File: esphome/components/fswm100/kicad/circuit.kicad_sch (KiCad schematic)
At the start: 17 parts, among them J1 Bi-Directional 3.3V-5V Shifte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, J2 ESP32 DEVKITV1 (ESP-WROOM-32), U1 ADS1115IDGS, U2 L7805, U3 TCRT5000, U4 L7805

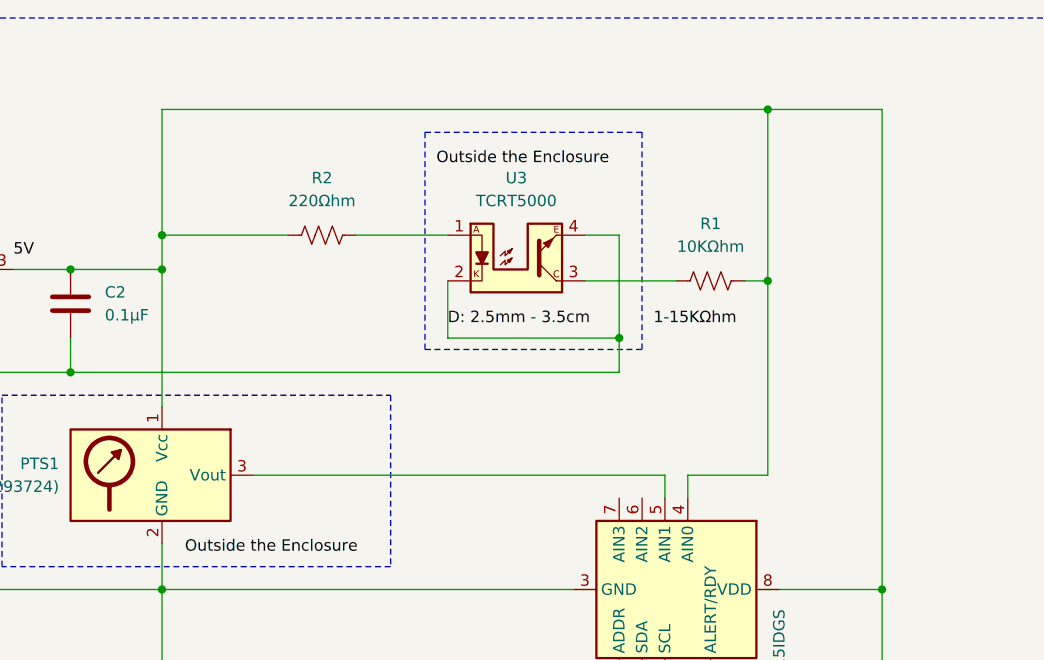
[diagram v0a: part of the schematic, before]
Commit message: fix flow sensor code and diagram
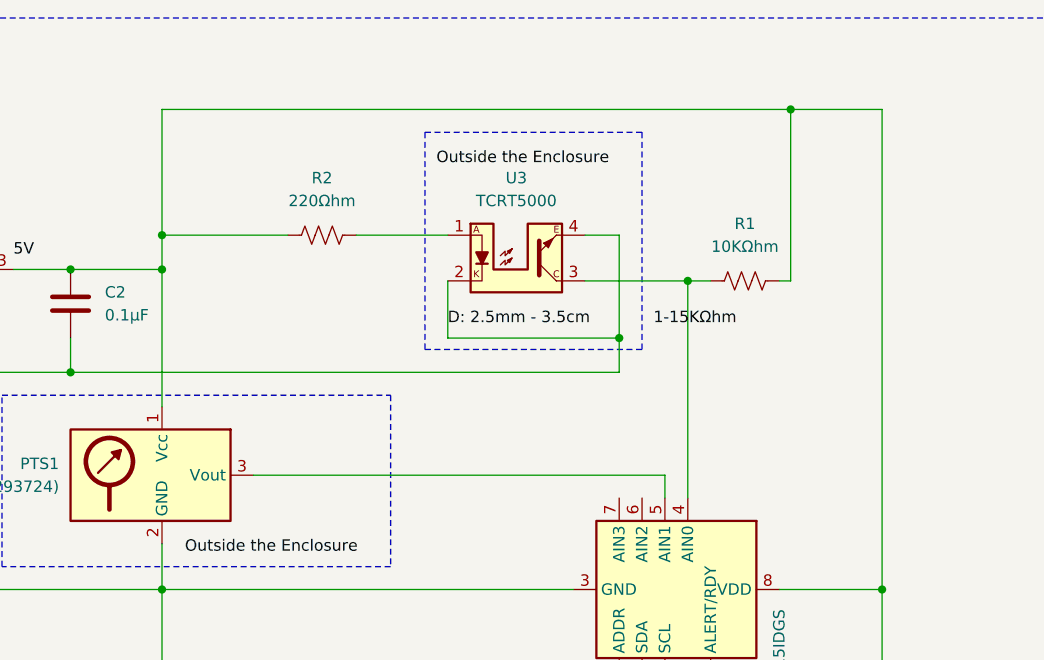
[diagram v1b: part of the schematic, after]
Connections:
- net at C2.1, J1.HV (3), PTS1.1 (Vcc)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: no longer U1.4 (AIN0)
- net at R1.2, U3.3: now also U1.4 (AIN0)
- new net: J1.GND (9), J2.GND (Pin_17), R3.2
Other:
- moved on the sheet: R1
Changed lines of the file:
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@@
-	)
-	(junction
-		(at 157.48 64.77)
-		(diameter 0)
-		(color 0 0 0 0)
 	)
 	(junction
@@
 	)
 	(junction
+		(at 148.59 64.77)
+		(diameter 0)
+		(color 0 0 0 0)
+	)
+	(junction
 		(at 39.37 74.93)
 		(diameter 0)
@@
 	)
 	(junction
-		(at 157.48 45.72)
-		(diameter 0)
-		(color 0 0 0 0)
-	)
-	(junction
 		(at 170.18 99.06)
 		(diameter 0)
@@
 	)
 	(junction
+		(at 160.02 45.72)
+		(diameter 0)
+		(color 0 0 0 0)
+	)
+	(junction
 		(at 49.53 74.93)
 		(diameter 0)
@@
 	(wire
 		(pts
-			(xy 137.16 64.77) (xy 147.32 64.77)
+			(xy 137.16 64.77) (xy 148.59 64.77)
 		)
 		(stroke
@@
 	(wire
 		(pts
+			(xy 151.13 64.77) (xy 148.59 64.77)
+		)
+		(stroke
+			(width 0)
+			(type default)
+		)
+	)
+	(wire
+		(pts
 			(xy 73.66 63.5) (xy 80.01 63.5)
 		)
@@
 	(wire
 		(pts
-			(xy 157.48 45.72) (xy 90.17 45.72)
+			(xy 90.17 45.72) (xy 160.02 45.72)
 		)
 		(stroke
@@
 	(wire
 		(pts
+			(xy 148.59 64.77) (xy 148.59 88.9)
+		)
+		(stroke
+			(width 0)
+			(type default)
+		)
+	)
+	(wire
+		(pts
 			(xy 236.22 151.13) (xy 261.62 151.13)
 		)
@@
 	(wire
 		(pts
-			(xy 148.59 88.9) (xy 148.59 86.36)
-		)
-		(stroke
-			(width 0)
-			(type default)
-		)
-	)
-	(wire
-		(pts
 			(xy 66.04 99.06) (xy 66.04 74.93)
 		)
@@
 	(wire
 		(pts
-			(xy 157.48 86.36) (xy 157.48 64.77)
-		)
-		(stroke
-			(width 0)
-			(type default)
-		)
-	)
-	(wire
-		(pts
 			(xy 257.81 59.69) (xy 261.62 59.69)
 		)
@@
 	(wire
 		(pts
-			(xy 157.48 45.72) (xy 170.18 45.72)
-		)
-		(stroke
-			(width 0)
-			(type default)
-		)
-	)
-	(wire
-		(pts
 			(xy 90.17 78.74) (xy 90.17 63.5)
 		)
@@
 	(wire
 		(pts
-			(xy 154.94 64.77) (xy 157.48 64.77)
+			(xy 158.75 64.77) (xy 160.02 64.77)
 		)
 		(stroke
@@
 	(wire
 		(pts
-			(xy 157.48 64.77) (xy 157.48 45.72)
+			(xy 160.02 64.77) (xy 160.02 45.72)
 		)
 		(stroke
@@
 	(wire
 		(pts
+			(xy 160.02 45.72) (xy 170.18 45.72)
+		)
+		(stroke
+			(width 0)
+			(type default)
+		)
+	)
+	(wire
+		(pts
 			(xy 170.18 130.81) (xy 170.18 99.06)
-		)
-		(stroke
-			(width 0)
-			(type default)
-		)
-	)
-	(wire
-		(pts
-			(xy 148.59 86.36) (xy 157.48 86.36)
 		)
 		(stroke
@@
 	(symbol
 		(lib_id "Device:R_US")
-		(at 151.13 64.77 270)
+		(at 154.94 64.77 270)
 		(unit 1)
 		(exclude_from_sim no)
@@
 		(fields_autoplaced yes)
 		(property "Reference" "R1"
-			(at 151.13 58.42 90)
+			(at 154.94 58.42 90)
 			(effects
 				(font
@@
 		)
 		(property "Value" "10KΩhm"
-			(at 151.13 60.96 90)
+			(at 154.94 60.96 90)
 			(effects
 				(font
@@
 		)
 		(property "Footprint" ""
-			(at 150.876 65.786 90)
+			(at 154.686 65.786 90)
 			(effects
 				(font
@@
 		)
 		(property "Datasheet" "~"
-			(at 151.13 64.77 0)
+			(at 154.94 64.77 0)
 			(effects
 				(font
@@
 		)
 		(property "Description" "Resistor, US symbol"
-			(at 151.13 64.77 0)
+			(at 154.94 64.77 0)
 			(effects
 				(font

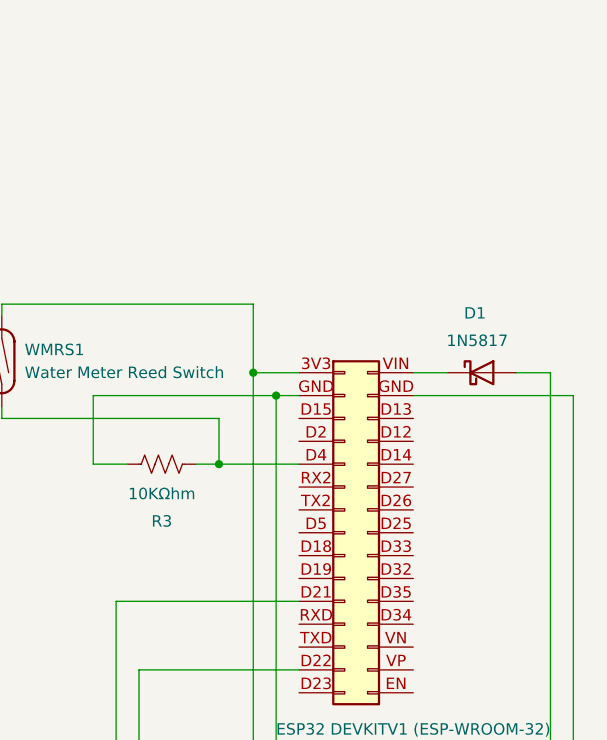
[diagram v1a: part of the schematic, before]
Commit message: add rgb status led to circuit
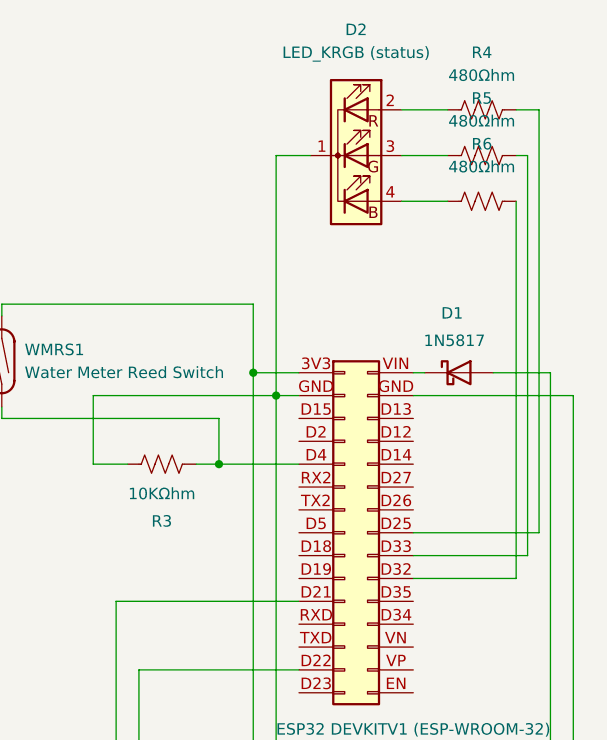
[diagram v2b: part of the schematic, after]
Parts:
- added D2: LED_KRGB (status), symbol Device:LED_KRGB
- added R4, R5, R6: 480Ωhm, symbol Device:R_US
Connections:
- net at J2.D25 (Pin_23): now also R4.2
- net at J2.D32 (Pin_25): now also R6.2
- net at J2.D33 (Pin_24): now also R5.2
- new net: D2.1 (K), J1.GND (9), J2.GND (Pin_17), R3.2
- new net: D2.2 (RA), R4.1
- new net: D2.3 (GA), R5.1
- new net: D2.4 (BA), R6.1
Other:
- moved on the sheet: D1
